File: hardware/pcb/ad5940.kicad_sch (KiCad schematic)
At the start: 18 parts, among them J6 EDA, U7 AD5940BCBZ

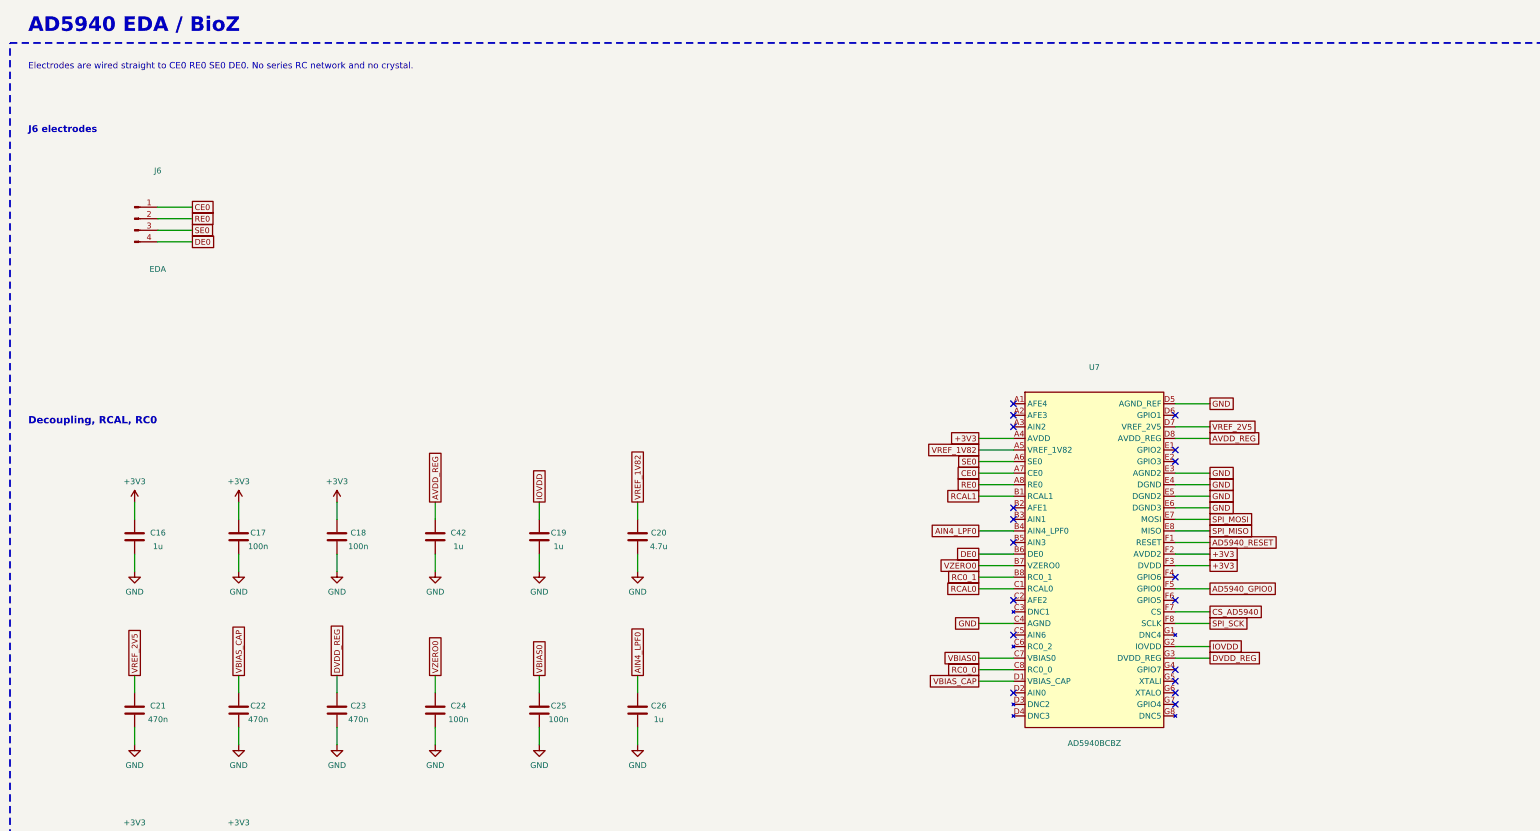
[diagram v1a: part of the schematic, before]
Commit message: Use official CAD and shrink the hw_v1 board to 37x30 mm.
Replace the hand-drawn AFE4900, AD5940, ADS1292R, AS7341, MLX90632,
TMP117, LSM6DSV80X, and MCP73831 symbols and footprints with the
SnapMagic and Ultra Librarian libraries. ADS1292R is now the QFN-32
ADS1292RIRSMT, and MLX90632SLD-DCB-100-SP moves SDA/SCL onto the
existing 1.8 V bus. Pin headers and mounting holes are flat solder
pads. The unrouted 4-layer placement keeps the antenna on the left
edge and the skin sensors together on the bottom.

Co-authored-by: Riyu-D1 <Riyu-D1@users.noreply.github.com>
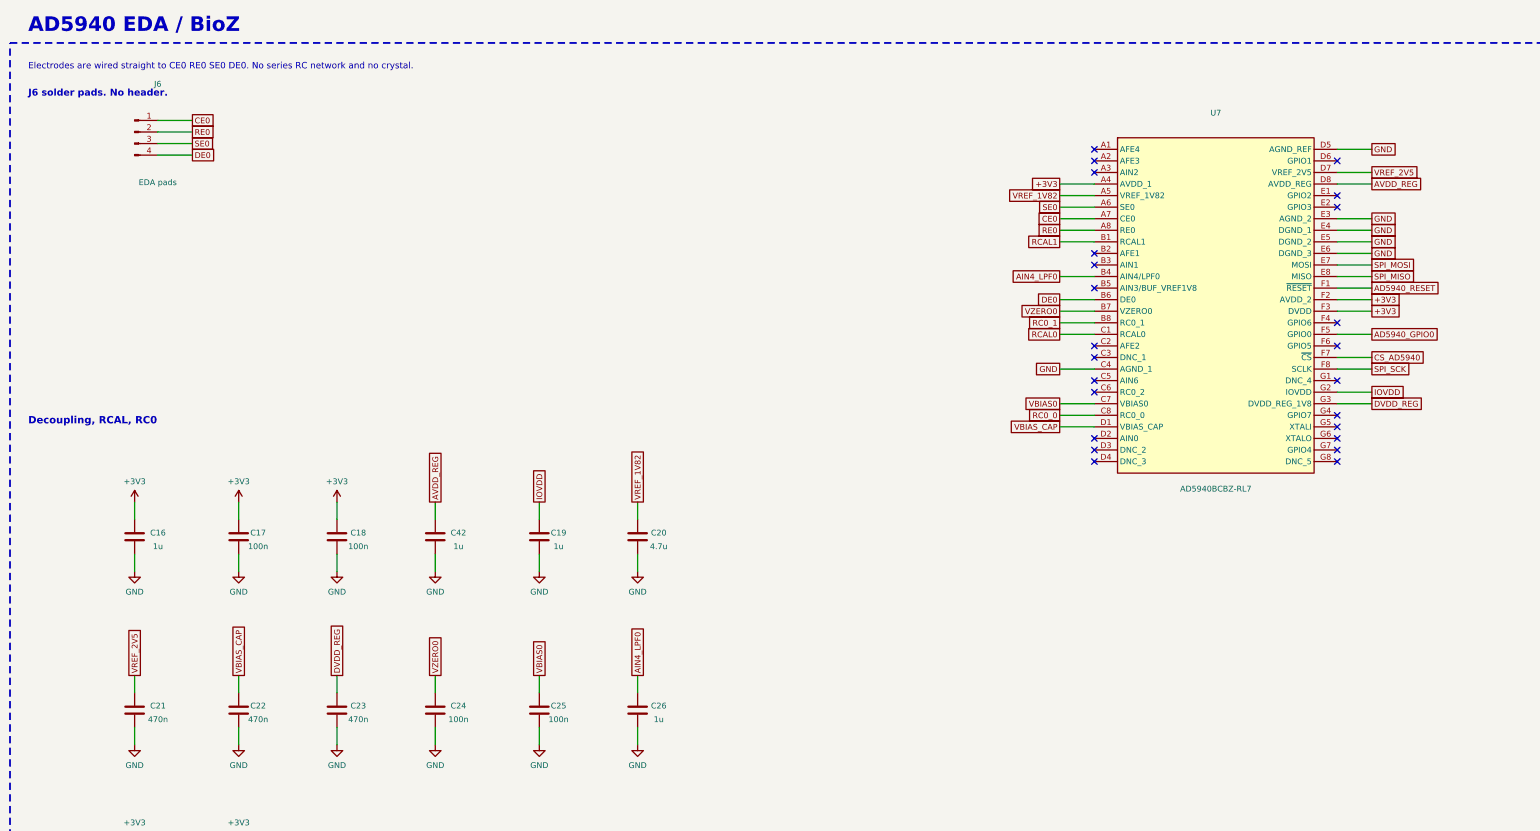
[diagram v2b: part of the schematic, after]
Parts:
- removed U7: AD5940BCBZ, vitalq:AD5940BCBZ, symbol vitalq:AD5940BCBZ
- added U7: AD5940BCBZ-RL7, snap:BGA56C40P8X7_416X356X55, symbol vitalq:AD5940BCBZ-RL7
- J6: value EDA -> EDA pads; footprint Connector_PinHeader_1.27mm:PinHeader_1x04_P1.27mm_Horizontal -> vitalq:Pads_EDA
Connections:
- net +3V3: now also U7.A4 (AVDD_1), U7.F2 (AVDD_2), U7.F3 (DVDD)
- net AD5940_GPIO0: now also U7.F5 (GPIO0)
- net AD5940_RESET: now also U7.F1 (~{RESET})
- net AIN4_LPF0: now also U7.B4 (AIN4/LPF0)
- net AVDD_REG: now also U7.D8 (AVDD_REG)
- net CE0: now also U7.A7 (CE0)
- net CS_AD5940: now also U7.F7 (~{CS})
- net DE0: now also U7.B6 (DE0)
- net DVDD_REG: now also U7.G3 (DVDD_REG_1V8)
- net GND: now also U7.C4 (AGND_1), U7.D5 (AGND_REF), U7.E3 (AGND_2), U7.E4 (DGND_1), U7.E5 (DGND_2), U7.E6 (DGND_3)
- net IOVDD: now also U7.G2 (IOVDD)
- net RC0_0: now also U7.C8 (RC0_0)
- net RC0_1: now also U7.B8 (RC0_1)
- net RCAL0: now also U7.C1 (RCAL0)
- net RCAL1: now also U7.B1 (RCAL1)
- net RE0: now also U7.A8 (RE0)
- net SE0: now also U7.A6 (SE0)
- net SPI_MISO: now also U7.E8 (MISO)
- net SPI_MOSI: now also U7.E7 (MOSI)
- net SPI_SCK: now also U7.F8 (SCLK)
- net VBIAS0: now also U7.C7 (VBIAS0)
- net VBIAS_CAP: now also U7.D1 (VBIAS_CAP)
- net VREF_1V82: now also U7.A5 (VREF_1V82)
- net VREF_2V5: now also U7.D7 (VREF_2V5)
- net VZERO0: now also U7.B7 (VZERO0)
- no-connect marks 18 -> 24
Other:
- note added: "J6 solder pads. No header."
- note removed: "J6 electrodes"

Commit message: Seat the QFN models and drop passives the datasheets do not require.
The ADS1292R STEP is already Z-up, so the extra X rotation stood the
4x4x1 mm body on edge. Remove TP1, TP2, C5, C12, C17, C31 and R4, add
the 1 uF AVDD bulk capacitor, and shorten the outline to 36.2 x 27.8 mm.

Co-authored-by: Riyu-D1 <Riyu-D1@users.noreply.github.com>
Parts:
- removed C17: 100n, Capacitor_SMD:C_0402_1005Metric, symbol vitalq:C
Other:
- note added: "C16 AVDD, C18 DVDD, C42 AVDD_REG, C19 IOVDD after R12, C20-C26 are the reference and bias caps."
- note removed: "C16+C17 AVDD, C18 DVDD, C42 AVDD_REG, C19 IOVDD after R12, C20-C26 are the reference and bias caps."

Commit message: Add the chest-board sensors and replace the 3.3 V LDO with a TPS63802.
The unrouted 40 x 34 mm board keeps every previous part except the off-board PPG pads, which the SFH 7072 replaces. Respiration, a second ECG lead, electrode protection, EDA, fuel gauge, flash, and the I/O expander are in the schematic.

Co-authored-by: Riyu-D1 <Riyu-D1@users.noreply.github.com>
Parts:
- added C54: 15n, Capacitor_SMD:C_0402_1005Metric, symbol vitalq:C
- added C55: 470n, Capacitor_SMD:C_0402_1005Metric, symbol vitalq:C
- added D6, D7, D8, D9: TPD1E10B06, vitalq:TPD1E10B06_DPY, symbol vitalq:D_TVS_2
- added R39, R40, R41, R42: 1k, Resistor_SMD:R_0402_1005Metric, symbol vitalq:R
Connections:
- net +3V3: no longer R11.1
- net AD5940_RESET: now also R11.1; no longer R11.2
- net CE0: now also R39.1; no longer J6.1 (Pin_1)
- net DE0: now also R42.1; no longer J6.4 (Pin_4)
- net GND: now also R11.2, D6.2, D7.2, D8.2, D9.2
- net RE0: now also R41.1; no longer J6.2 (Pin_2)
- net SE0: now also C55.1; no longer J6.3 (Pin_3)
- new net CE_ISO: C54.1, R39.2
- new net EDA_CE_PAD: C54.2, D6.1, J6.1 (Pin_1)
- new net EDA_DE_PAD: D9.1, J6.4 (Pin_4), R42.2
- new net EDA_RE_PAD: D8.1, J6.2 (Pin_2), R41.2
- new net EDA_SE_PAD: D7.1, J6.3 (Pin_3), R40.2
- new net SE_ISO: C55.2, R40.1
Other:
- note added: "Fig 54 / AN-1557: 1k and 15 nF in series on CE0, 470 nF on SE0, plus RCAL. Flex notes are in the README."
- note added: "RLIMIT is R39. CISO1 is C54. CISO2 is C55. R13 stays the 1k RCAL. D6-D9 are at the electrode pads."
- note removed: "DC skin conductance and the AC impedance network are not fitted. J6 is a direct electrode header."
- note removed: "Electrodes are wired straight to CE0 RE0 SE0 DE0. No series RC network and no crystal."

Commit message: Add defibrillator clamps and a charge-temperature cut-off.
Series electrode resistors are now DPCR2512 51k pulse parts, with an S30-A90X gas discharge tube on each patient pad ahead of the existing TPD1E10B06. The MCP73831 stays; a PicoStar FET floats PROG until firmware enables charge, and a 3-pin cell pad feeds a 10k NTC into GPIO39.

Co-authored-by: Riyu-D1 <Riyu-D1@users.noreply.github.com>
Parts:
- added D17, D18, D19, D20: S30-A90X, vitalq:GDT_S30, symbol vitalq:GDT
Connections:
- net CE_ISO: now also D6.1
- net DE0: now also D9.1
- net EDA_CE_PAD: now also D17.1; no longer D6.1
- net EDA_DE_PAD: now also D20.1; no longer D9.1
- net EDA_RE_PAD: now also D19.1; no longer D8.1
- net EDA_SE_PAD: now also D18.1; no longer D7.1
- net GND: now also D17.2, D18.2, D19.2, D20.2
- net RE0: now also D8.1
- net SE_ISO: now also D7.1
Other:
- note added: "RLIMIT is R39. CISO1 is C54. CISO2 is C55. R13 stays the 1k RCAL. D17-D20 are on the pads."
- note removed: "RLIMIT is R39. CISO1 is C54. CISO2 is C55. R13 stays the 1k RCAL. D6-D9 are at the electrode pads."
